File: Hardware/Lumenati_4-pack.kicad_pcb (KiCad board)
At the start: 2 copper layers, 21.6 x 21.6 mm, 22 parts, among them J1 5V, J2 CI, J3 DI, J4 GND, J5 CO, J6 DO, J7 5V, J8 GND, U1 APA102C, U2 APA102C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

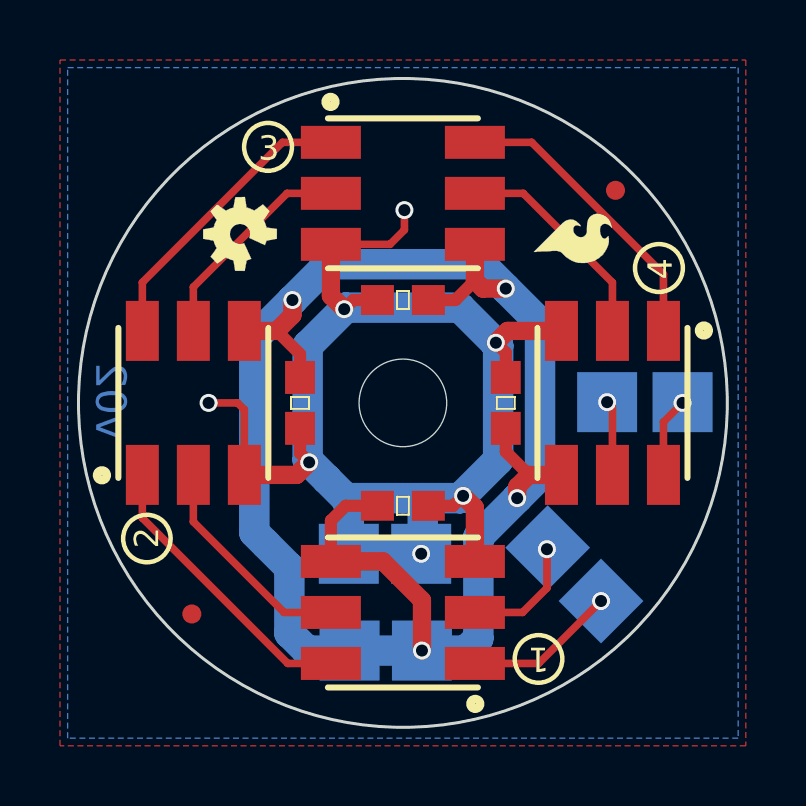
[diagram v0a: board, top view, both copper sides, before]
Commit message: Changed all the names to Lumenati, updated version to v10.
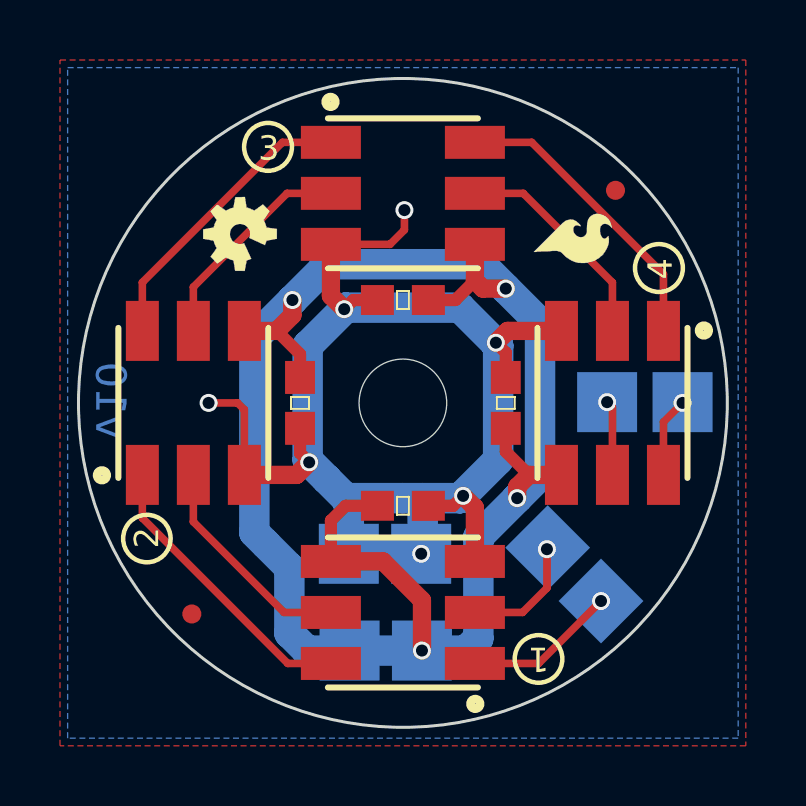
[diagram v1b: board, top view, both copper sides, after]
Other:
- board text added: "Lumenati 4-pack"
- board text added: "v10"
- board text removed: "HiBeam 4-pack"
- board text removed: "HiBeams 4-pack"
- board text removed: "v02"
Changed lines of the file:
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@@
   (layers
     (0 F.Cu signal hide)
-    (31 B.Cu signal hide)
+    (31 B.Cu signal)
     (32 B.Adhes user)
     (33 F.Adhes user)
@@
     (effects (font (size 0.8128 0.8128) (thickness 0.1778)))
   )
-  (gr_text 5/8/17 (at 211.328 192.9638) (layer Dwgs.User)
+  (gr_text 5/8/17 (at 211.328 192.9638) (layer Cmts.User)
     (effects (font (size 1.5 1.5) (thickness 0.3)))
   )
-  (gr_text v02 (at 270.51 193.1162) (layer Dwgs.User)
+  (gr_text v10 (at 270.51 193.1162) (layer Cmts.User)
     (effects (font (size 1.5 1.5) (thickness 0.3)))
   )
-  (gr_text 1/1 (at 187.8584 183.0578) (layer Dwgs.User)
+  (gr_text 1/1 (at 187.8584 183.0578) (layer Cmts.User)
     (effects (font (size 1.5 1.5) (thickness 0.3)))
   )
-  (gr_text "HiBeam 4-pack" (at 196.469 189.4586) (layer Dwgs.User)
+  (gr_text "Lumenati 4-pack" (at 196.469 189.4586) (layer Cmts.User)
     (effects (font (size 1.5 1.5) (thickness 0.3)))
   )
-  (gr_text "Released under the Creative Commons\nAttribution Share-Alike 4.0 License\nhttps://creativecommons.org/licenses/by-sa/4.0/\nDesigned by Pete Dokter" (at 179.451 173.7868) (layer Dwgs.User)
+  (gr_text "Released under the Creative Commons\nAttribution Share-Alike 4.0 License\nhttps://creativecommons.org/licenses/by-sa/4.0/\nDesigned by Pete Dokter" (at 179.451 173.7868) (layer Cmts.User)
     (effects (font (size 1.5 1.5) (thickness 0.3)) (justify left))
   )
@@
   (gr_line (start 135.1026 111.76) (end 135.1026 101.6) (angle 90) (layer Dwgs.User) (width 0.2))
   (gr_line (start 156.7434 111.76) (end 156.7434 101.6) (angle 90) (layer Dwgs.User) (width 0.2))
-  (gr_text v02 (at 136.1694 98.3488 270) (layer B.Cu)
+  (gr_text v10 (at 136.1694 98.3488 270) (layer B.Cu)
     (effects (font (size 1.016 1.016) (thickness 0.2032)) (justify mirror))
   )
-  (gr_text "HiBeams 4-pack" (at 145.796 93.6752) (layer B.SilkS)
+  (gr_text "Lumenati 4-pack" (at 145.796 93.6752) (layer B.SilkS)
     (effects (font (size 1.27 1.27) (thickness 0.2032)) (justify mirror))
   )
